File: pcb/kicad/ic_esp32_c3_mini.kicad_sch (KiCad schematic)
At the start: 5 parts, among them U1 ESP32-C3-MINI-1

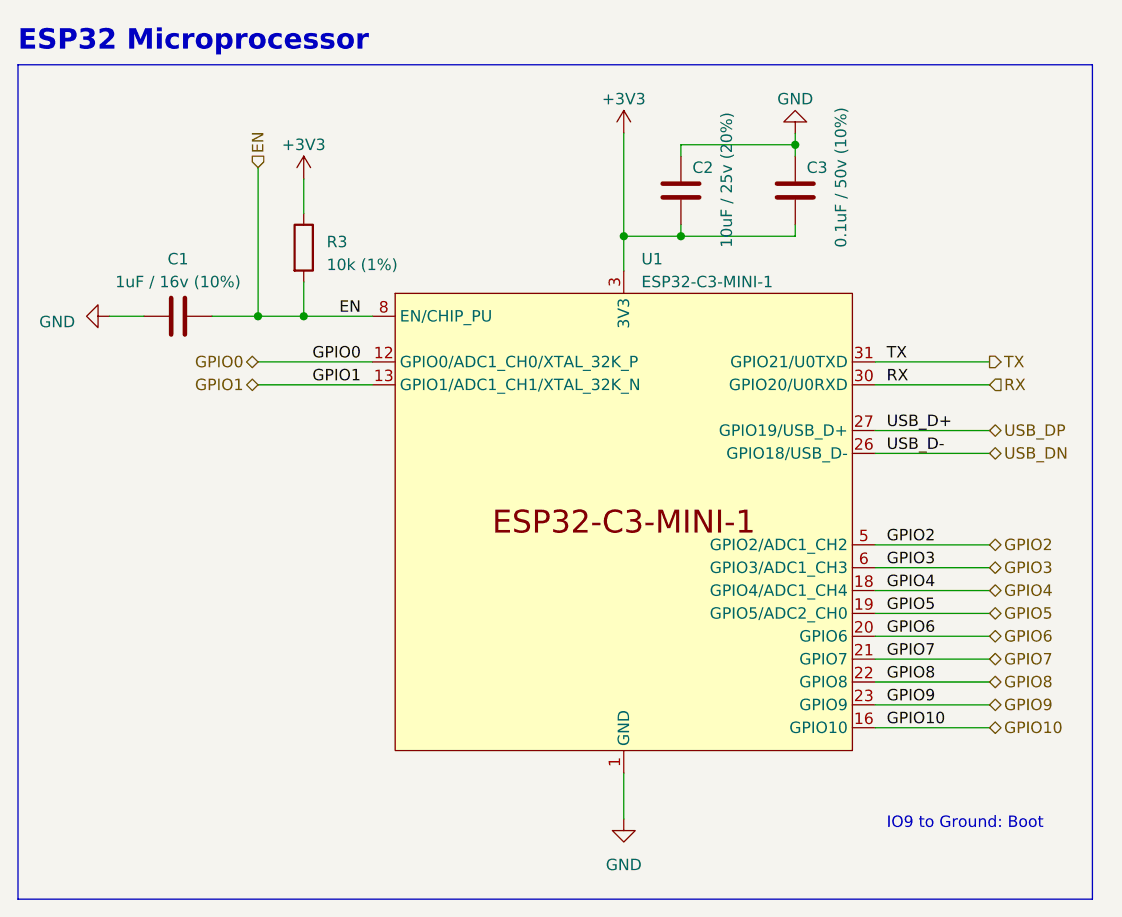
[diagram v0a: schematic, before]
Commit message: Rev 2 Update
Change Log:
- added I2C header
- added GPIO header (IO0, IO4, IO5, IO10)
- added 10k pull-up on IO8
- added label on USB C port
- added kwartzlab logo to the silk screen layer
- fixed some traces
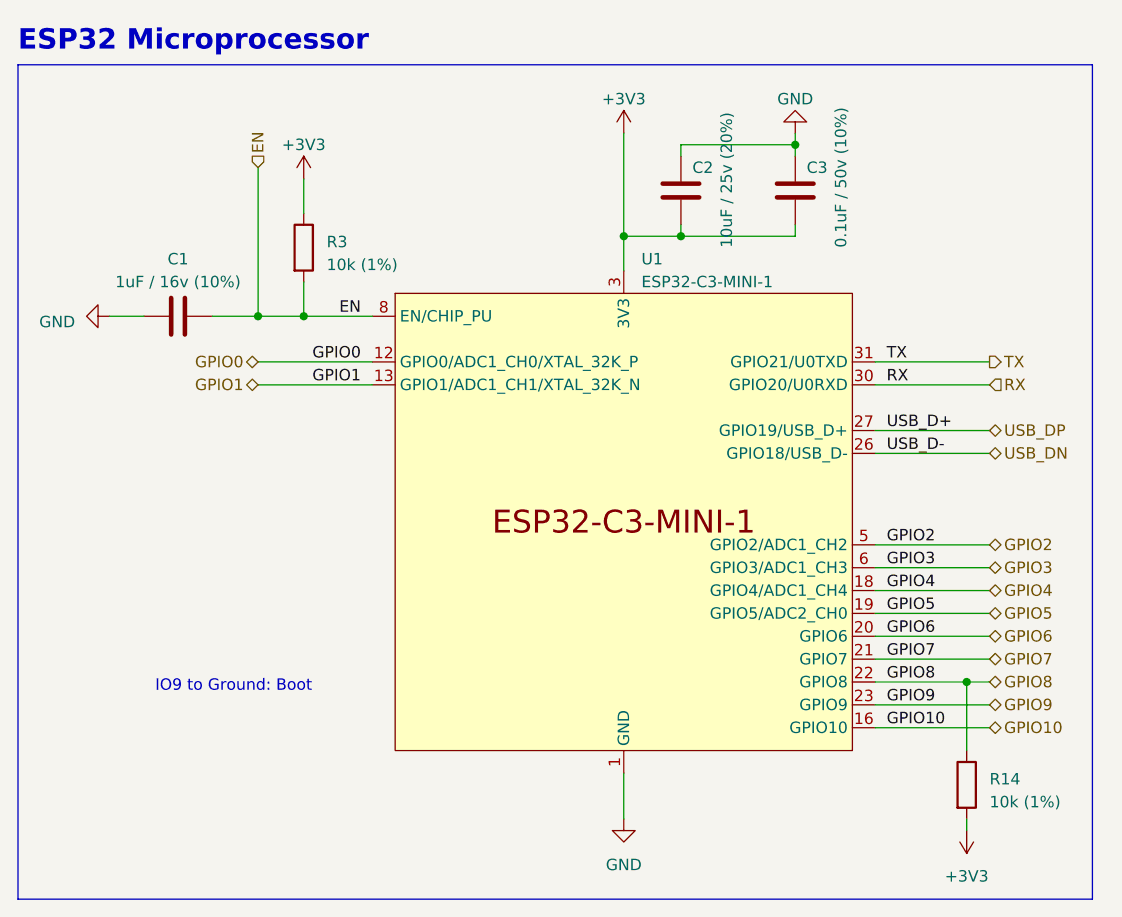
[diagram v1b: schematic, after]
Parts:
- added R14: 10k (1%), PCM_Resistor_SMD_AKL:R_0603_1608Metric, symbol Device:R
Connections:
- net +3V3: now also R14.2
- net GPIO8: now also R14.1
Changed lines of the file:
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@@
   (title_block
     (title "Kwartzlab Environmental Sensor")
-    (date "2023-03-24")
-    (rev "1")
+    (date "2023-04-04")
+    (rev "2")
     (company "Created By: Erin Reed (FireLabs - www.firelabs.ca)")
   )
@@
   (junction (at 158.75 74.93) (diameter 0) (color 0 0 0 0)
   )
+  (junction (at 190.5 124.46) (diameter 0) (color 0 0 0 0)
+  )
   (wire (pts (xy 180.34 127) (xy 193.04 127))
     (stroke (width 0) (type default))
@@
     (stroke (width 0) (type default))
   )
+  (wire (pts (xy 190.5 139.7) (xy 190.5 140.97))
+    (stroke (width 0) (type default))
+  )
   (wire (pts (xy 158.75 64.77) (xy 158.75 66.04))
     (stroke (width 0) (type default))
@@
     (stroke (width 0) (type default))
   )
+  (wire (pts (xy 190.5 124.46) (xy 193.04 124.46))
+    (stroke (width 0) (type default))
+  )
   (wire (pts (xy 180.34 111.76) (xy 193.04 111.76))
     (stroke (width 0) (type default))
   )
-  (wire (pts (xy 180.34 124.46) (xy 193.04 124.46))
+  (wire (pts (xy 190.5 124.46) (xy 190.5 132.08))
+    (stroke (width 0) (type default))
+  )
+  (wire (pts (xy 180.34 124.46) (xy 190.5 124.46))
     (stroke (width 0) (type default))
   )
@@
     (fill (type none))
   )
-  (text "IO9 to Ground: Boot " (at 181.61 140.97 0)
+  (text "IO9 to Ground: Boot " (at 100.33 125.73 0)
     (effects (font (size 1.27 1.27)) (justify left bottom))
   )
@@
     (pin "2")
     (instances
-      (project "KwartzLab-SensorBoard-Rev1"
+      (project "KwartzLab-SensorBoard-Rev2"
         (path "/02789d54-6086-45b9-8196-8325e6f33099/2426fcd9-5a43-41a7-b855-a8909e878faf"
           (reference "C2") (unit 1)
@@
     (pin "1")
     (instances
-      (project "KwartzLab-SensorBoard-Rev1"
+      (project "KwartzLab-SensorBoard-Rev2"
         (path "/02789d54-6086-45b9-8196-8325e6f33099/2426fcd9-5a43-41a7-b855-a8909e878faf"
           (reference "#PWR016") (unit 1)
@@
     (pin "1")
     (instances
-      (project "KwartzLab-SensorBoard-Rev1"
+      (project "KwartzLab-SensorBoard-Rev2"
         (path "/02789d54-6086-45b9-8196-8325e6f33099/2426fcd9-5a43-41a7-b855-a8909e878faf"
           (reference "#PWR014") (unit 1)
@@
     (pin "9")
     (instances
-      (project "KwartzLab-SensorBoard-Rev1"
+      (project "KwartzLab-SensorBoard-Rev2"
         (path "/02789d54-6086-45b9-8196-8325e6f33099/2426fcd9-5a43-41a7-b855-a8909e878faf"
           (reference "U1") (unit 1)
@@
     (pin "1")
     (instances
-      (project "KwartzLab-SensorBoard-Rev1"
+      (project "KwartzLab-SensorBoard-Rev2"
         (path "/02789d54-6086-45b9-8196-8325e6f33099/2426fcd9-5a43-41a7-b855-a8909e878faf"
           (reference "#PWR017") (unit 1)
@@
     (pin "1")
     (instances
-      (project "KwartzLab-SensorBoard-Rev1"
+      (project "KwartzLab-SensorBoard-Rev2"
         (path "/02789d54-6086-45b9-8196-8325e6f33099/2426fcd9-5a43-41a7-b855-a8909e878faf"
           (reference "#PWR015") (unit 1)
@@
     (pin "2")
     (instances
-      (project "KwartzLab-SensorBoard-Rev1"
+      (project "KwartzLab-SensorBoard-Rev2"
         (path "/02789d54-6086-45b9-8196-8325e6f33099/2426fcd9-5a43-41a7-b855-a8909e878faf"
           (reference "C3") (unit 1)
@@
         (path "/e97df847-49dd-43a4-b7f5-00448f4c7aca"
           (reference "C?") (unit 1)
+        )
+      )
+    )
+  )
+  (symbol (lib_id "Device:R") (at 190.5 135.89 0) (unit 1)
+    (in_bom yes) (on_board yes) (dnp no) (fields_autoplaced)
+    (property "Reference" "R14" (at 193.04 135.255 0)
+      (effects (font (size 1.27 1.27)) (justify left))
+    )
+    (property "Value" "10k (1%)" (at 193.04 137.795 0)
+      (effects (font (size 1.27 1.27)) (justify left))
+    )
+    (property "Footprint" "PCM_Resistor_SMD_AKL:R_0603_1608Metric" (at 188.722 135.89 90)
+      (effects (font (size 1.27 1.27)) hide)
+    )
+    (property "Datasheet" "~" (at 190.5 135.89 0)
+      (effects (font (size 1.27 1.27)) hide)
+    )
+    (pin "1")
+    (pin "2")
+    (instances
+      (project "KwartzLab-SensorBoard-Rev2"
+        (path "/02789d54-6086-45b9-8196-8325e6f33099/2426fcd9-5a43-41a7-b855-a8909e878faf"
+          (reference "R14") (unit 1)
+        )
+      )
+      (project "ic_esp32_wroom_32"
+        (path "/836076e6-9e6b-40f6-ae50-4a2b99b36357"
+          (reference "R1") (unit 1)
+        )
+      )
+      (project "ic_esp32_c3_mini"
+        (path "/e97df847-49dd-43a4-b7f5-00448f4c7aca"
+          (reference "R?") (unit 1)
         )
       )
@@
     (pin "2")
     (instances
-      (project "KwartzLab-SensorBoard-Rev1"
+      (project "KwartzLab-SensorBoard-Rev2"
         (path "/02789d54-6086-45b9-8196-8325e6f33099/2426fcd9-5a43-41a7-b855-a8909e878faf"
           (reference "C1") (unit 1)
@@
     (pin "2")
     (instances
-      (project "KwartzLab-SensorBoard-Rev1"
+      (project "KwartzLab-SensorBoard-Rev2"
         (path "/02789d54-6086-45b9-8196-8325e6f33099/2426fcd9-5a43-41a7-b855-a8909e878faf"
           (reference "R3") (unit 1)
@@
     (pin "1")
     (instances
-      (project "KwartzLab-SensorBoard-Rev1"
+      (project "KwartzLab-SensorBoard-Rev2"
         (path "/02789d54-6086-45b9-8196-8325e6f33099/2426fcd9-5a43-41a7-b855-a8909e878faf"
           (reference "#PWR013") (unit 1)
@@
         )
       )
+    )
+  )
+  (symbol (lib_id "power:+3V3") (at 190.5 140.97 180) (unit 1)
+    (in_bom yes) (on_board yes) (dnp no) (fields_autoplaced)
+    (property "Reference" "#PWR059" (at 190.5 137.16 0)
+      (effects (font (size 1.27 1.27)) hide)
+    )
+    (property "Value" "+3V3" (at 190.5 146.05 0)
+      (effects (font (size 1.27 1.27)))
+    )
+    (property "Footprint" "" (at 190.5 140.97 0)
+      (effects (font (size 1.27 1.27)) hide)
+    )
+    (property "Datasheet" "" (at 190.5 140.97 0)
+      (effects (font (size 1.27 1.27)) hide)
+    )
+    (pin "1")
+    (instances
+      (project "KwartzLab-SensorBoard-Rev2"
+        (path "/02789d54-6086-45b9-8196-8325e6f33099/2426fcd9-5a43-41a7-b855-a8909e878faf"
+          (reference "#PWR059") (unit 1)
+        )
+      )
